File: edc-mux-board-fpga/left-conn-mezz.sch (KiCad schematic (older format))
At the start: 86 parts

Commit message: finished draft of horizontal pcb connector pinout.
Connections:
- net +12V: now also J?.37 (Pin_37), J?.38 (Pin_38); no longer J?.45 (Pin_45), J?.46 (Pin_46)
- net AUD_GND0: now also J?.5 (Pin_5); no longer J?.7 (Pin_7)
- net AUD_GND1: now also J?.17 (Pin_17); no longer J?.19 (Pin_19)
- net AUD_GND2: now also J?.29 (Pin_29); no longer J?.31 (Pin_31)
- net AUD_GND3: now also J?.51 (Pin_51); no longer J?.54 (Pin_54)
- net AUD_GND4: now also J?.63 (Pin_63); no longer J?.65 (Pin_65)
- net AUD_GND5: now also J?.75 (Pin_75); no longer J?.74 (Pin_74)
- net GND: now also J?.11 (Pin_11), J?.18 (Pin_18), J?.23 (Pin_23), J?.24 (Pin_24), J?.30 (Pin_30), J?.45 (Pin_45), J?.46 (Pin_46), J?.52 (Pin_52), J?.57 (Pin_57), J?.58 (Pin_58), J?.64 (Pin_64), J?.69 (Pin_69), J?.70 (Pin_70), J?.76 (Pin_76); no longer J?.1 (Pin_1), J?.13 (Pin_13), J?.22 (Pin_22), J?.25 (Pin_25), J?.33 (Pin_33), J?.37 (Pin_37), J?.38 (Pin_38), J?.47 (Pin_47), J?.48 (Pin_48), J?.49 (Pin_49), J?.59 (Pin_59), J?.68 (Pin_68), J?.75 (Pin_75), J?.80 (Pin_80)
- net ID_PIN0: now also J?.9 (Pin_9); no longer J?.10 (Pin_10)
- net ID_PIN1: now also J?.21 (Pin_21); no longer J?.20 (Pin_20)
- net ID_PIN2: now also J?.33 (Pin_33); no longer J?.26 (Pin_26)
- net ID_PIN3: now also J?.55 (Pin_55); no longer J?.51 (Pin_51)
- net ID_PIN4: now also J?.67 (Pin_67); no longer J?.60 (Pin_60)
- net ID_PIN5: now also J?.79 (Pin_79); no longer J?.71 (Pin_71)
- net INT_0: now also J?.7 (Pin_7); no longer J?.8 (Pin_8)
- net INT_1: now also J?.19 (Pin_19); no longer J?.18 (Pin_18)
- net INT_2: now also J?.31 (Pin_31); no longer J?.24 (Pin_24)
- net INT_4: now also J?.65 (Pin_65); no longer J?.62 (Pin_62)
- net INT_5: now also J?.77 (Pin_77); no longer J?.73 (Pin_73)
- net L_IN0: now also J?.3 (Pin_3); no longer J?.5 (Pin_5)
- net L_IN1: now also J?.15 (Pin_15); no longer J?.14 (Pin_14)
- net L_IN2: now also J?.27 (Pin_27); no longer J?.28 (Pin_28)
- net L_IN3: now also J?.49 (Pin_49); no longer J?.56 (Pin_56)
- net L_IN4: now also J?.61 (Pin_61); no longer J?.67 (Pin_67)
- net L_IN5: now also J?.73 (Pin_73); no longer J?.76 (Pin_76)
- net L_OUT0: now also J?.4 (Pin_4); no longer J?.2 (Pin_2)
- net L_OUT1: now also J?.16 (Pin_16); no longer J?.17 (Pin_17)
- net L_OUT2: now also J?.28 (Pin_28); no longer J?.32 (Pin_32)
- net L_OUT3: now also J?.50 (Pin_50); no longer J?.57 (Pin_57)
- net L_OUT4: now also J?.62 (Pin_62); no longer J?.64 (Pin_64)
- net L_OUT5: now also J?.74 (Pin_74); no longer J?.79 (Pin_79)
- net M_+12V: now also J?.37 (Pin_37), J?.38 (Pin_38); no longer J?.45 (Pin_45), J?.46 (Pin_46)
- net M_AUD_GND0: now also J?.5 (Pin_5); no longer J?.7 (Pin_7)
- net M_AUD_GND1: now also J?.17 (Pin_17); no longer J?.19 (Pin_19)
- net M_AUD_GND2: now also J?.29 (Pin_29); no longer J?.31 (Pin_31)
- net M_AUD_GND3: now also J?.51 (Pin_51); no longer J?.54 (Pin_54)
- net M_AUD_GND4: now also J?.63 (Pin_63); no longer J?.65 (Pin_65)
- net M_AUD_GND5: now also J?.75 (Pin_75); no longer J?.74 (Pin_74)
- net M_GND: now also J?.11 (Pin_11), J?.18 (Pin_18), J?.23 (Pin_23), J?.24 (Pin_24), J?.30 (Pin_30), J?.45 (Pin_45), J?.46 (Pin_46), J?.52 (Pin_52), J?.57 (Pin_57), J?.58 (Pin_58), J?.64 (Pin_64), J?.69 (Pin_69), J?.70 (Pin_70), J?.76 (Pin_76); no longer J?.1 (Pin_1), J?.13 (Pin_13), J?.22 (Pin_22), J?.25 (Pin_25), J?.33 (Pin_33), J?.37 (Pin_37), J?.38 (Pin_38), J?.47 (Pin_47), J?.48 (Pin_48), J?.49 (Pin_49), J?.59 (Pin_59), J?.68 (Pin_68), J?.75 (Pin_75), J?.80 (Pin_80)
- net M_ID_PIN0: now also J?.9 (Pin_9); no longer J?.10 (Pin_10)
- net M_ID_PIN1: now also J?.21 (Pin_21); no longer J?.20 (Pin_20)
- net M_ID_PIN2: now also J?.33 (Pin_33); no longer J?.26 (Pin_26)
- net M_ID_PIN3: now also J?.55 (Pin_55); no longer J?.51 (Pin_51)
- net M_ID_PIN4: now also J?.67 (Pin_67); no longer J?.60 (Pin_60)
- net M_ID_PIN5: now also J?.79 (Pin_79); no longer J?.71 (Pin_71)
- net M_INT_0: now also J?.7 (Pin_7); no longer J?.8 (Pin_8)
- net M_INT_1: now also J?.19 (Pin_19); no longer J?.18 (Pin_18)
- net M_INT_2: now also J?.31 (Pin_31); no longer J?.24 (Pin_24)
- net M_INT_4: now also J?.65 (Pin_65); no longer J?.62 (Pin_62)
- net M_INT_5: now also J?.77 (Pin_77); no longer J?.73 (Pin_73)
- net M_L_IN0: now also J?.3 (Pin_3); no longer J?.5 (Pin_5)
- net M_L_IN1: now also J?.15 (Pin_15); no longer J?.14 (Pin_14)
- net M_L_IN2: now also J?.27 (Pin_27); no longer J?.28 (Pin_28)
- net M_L_IN3: now also J?.49 (Pin_49); no longer J?.56 (Pin_56)
- net M_L_IN4: now also J?.61 (Pin_61); no longer J?.67 (Pin_67)
- net M_L_IN5: now also J?.73 (Pin_73); no longer J?.76 (Pin_76)
- net M_L_OUT1: now also J?.16 (Pin_16); no longer J?.15 (Pin_15)
- net M_L_OUT2: now also J?.28 (Pin_28); no longer J?.32 (Pin_32)
- net M_L_OUT3: now also J?.50 (Pin_50); no longer J?.57 (Pin_57)
- net M_L_OUT4: now also J?.62 (Pin_62); no longer J?.64 (Pin_64)
- net M_L_OUT5: now also J?.74 (Pin_74); no longer J?.79 (Pin_79)
- net M_R_IN0: now also J?.1 (Pin_1); no longer J?.3 (Pin_3)
- net M_R_IN1: now also J?.13 (Pin_13); no longer J?.16 (Pin_16)
- net M_R_IN2: now also J?.25 (Pin_25); no longer J?.30 (Pin_30)
- net M_R_IN3: now also J?.47 (Pin_47); no longer J?.58 (Pin_58)
- net M_R_IN4: now also J?.59 (Pin_59); no longer J?.69 (Pin_69)
- net M_R_IN5: now also J?.71 (Pin_71); no longer J?.78 (Pin_78)
- net M_R_OUT1: now also J?.14 (Pin_14); no longer J?.17 (Pin_17)
- net M_R_OUT2: now also J?.26 (Pin_26); no longer J?.34 (Pin_34)
- net M_R_OUT3: now also J?.48 (Pin_48); no longer J?.55 (Pin_55)
- net M_R_OUT4: now also J?.60 (Pin_60); no longer J?.66 (Pin_66)
- net M_R_OUT5: now also J?.72 (Pin_72); no longer J?.77 (Pin_77)
- net M_SCL_HV0: now also J?.8 (Pin_8); no longer J?.11 (Pin_11)
- net M_SCL_HV1: now also J?.20 (Pin_20); no longer J?.23 (Pin_23)
- net M_SCL_HV2: now also J?.32 (Pin_32); no longer J?.27 (Pin_27)
- net M_SCL_HV3: now also J?.54 (Pin_54); no longer J?.52 (Pin_52)
- net M_SCL_HV4: now also J?.66 (Pin_66); no longer J?.61 (Pin_61)
- net M_SCL_HV5: now also J?.78 (Pin_78); no longer J?.70 (Pin_70)
- net M_SDA_HV0: now also J?.10 (Pin_10); no longer J?.9 (Pin_9)
- net M_SDA_HV1: now also J?.22 (Pin_22); no longer J?.21 (Pin_21)
- net M_SDA_HV2: now also J?.34 (Pin_34); no longer J?.29 (Pin_29)
- net M_SDA_HV3: now also J?.56 (Pin_56); no longer J?.50 (Pin_50)
- net M_SDA_HV4: now also J?.68 (Pin_68); no longer J?.63 (Pin_63)
- net M_SDA_HV5: now also J?.80 (Pin_80); no longer J?.72 (Pin_72)
- net R_IN0: now also J?.1 (Pin_1); no longer J?.3 (Pin_3)
- net R_IN1: now also J?.13 (Pin_13); no longer J?.16 (Pin_16)
- net R_IN2: now also J?.25 (Pin_25); no longer J?.30 (Pin_30)
- net R_IN3: now also J?.47 (Pin_47); no longer J?.58 (Pin_58)
- net R_IN4: now also J?.59 (Pin_59); no longer J?.69 (Pin_69)
- net R_IN5: now also J?.71 (Pin_71); no longer J?.78 (Pin_78)
- net R_OUT0: now also J?.2 (Pin_2); no longer J?.4 (Pin_4)
- net R_OUT1: now also J?.14 (Pin_14); no longer J?.15 (Pin_15)
- net R_OUT2: now also J?.26 (Pin_26); no longer J?.34 (Pin_34)
- net R_OUT3: now also J?.48 (Pin_48); no longer J?.55 (Pin_55)
- net R_OUT4: now also J?.60 (Pin_60); no longer J?.66 (Pin_66)
- net R_OUT5: now also J?.72 (Pin_72); no longer J?.77 (Pin_77)
- net SCL_HV0: now also J?.8 (Pin_8); no longer J?.11 (Pin_11)
- net SCL_HV1: now also J?.20 (Pin_20); no longer J?.23 (Pin_23)
- net SCL_HV2: now also J?.32 (Pin_32); no longer J?.27 (Pin_27)
- net SCL_HV3: now also J?.54 (Pin_54); no longer J?.52 (Pin_52)
- net SCL_HV4: now also J?.66 (Pin_66); no longer J?.61 (Pin_61)
- net SCL_HV5: now also J?.78 (Pin_78); no longer J?.70 (Pin_70)
- net SDA_HV0: now also J?.10 (Pin_10); no longer J?.9 (Pin_9)
- net SDA_HV1: now also J?.22 (Pin_22); no longer J?.21 (Pin_21)
- net SDA_HV2: now also J?.34 (Pin_34); no longer J?.29 (Pin_29)
- net SDA_HV3: now also J?.56 (Pin_56); no longer J?.50 (Pin_50)
- net SDA_HV4: now also J?.68 (Pin_68); no longer J?.63 (Pin_63)
- net SDA_HV5: now also J?.80 (Pin_80); no longer J?.72 (Pin_72)
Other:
- moved on the sheet: C?, D?, F?, FB?, J?

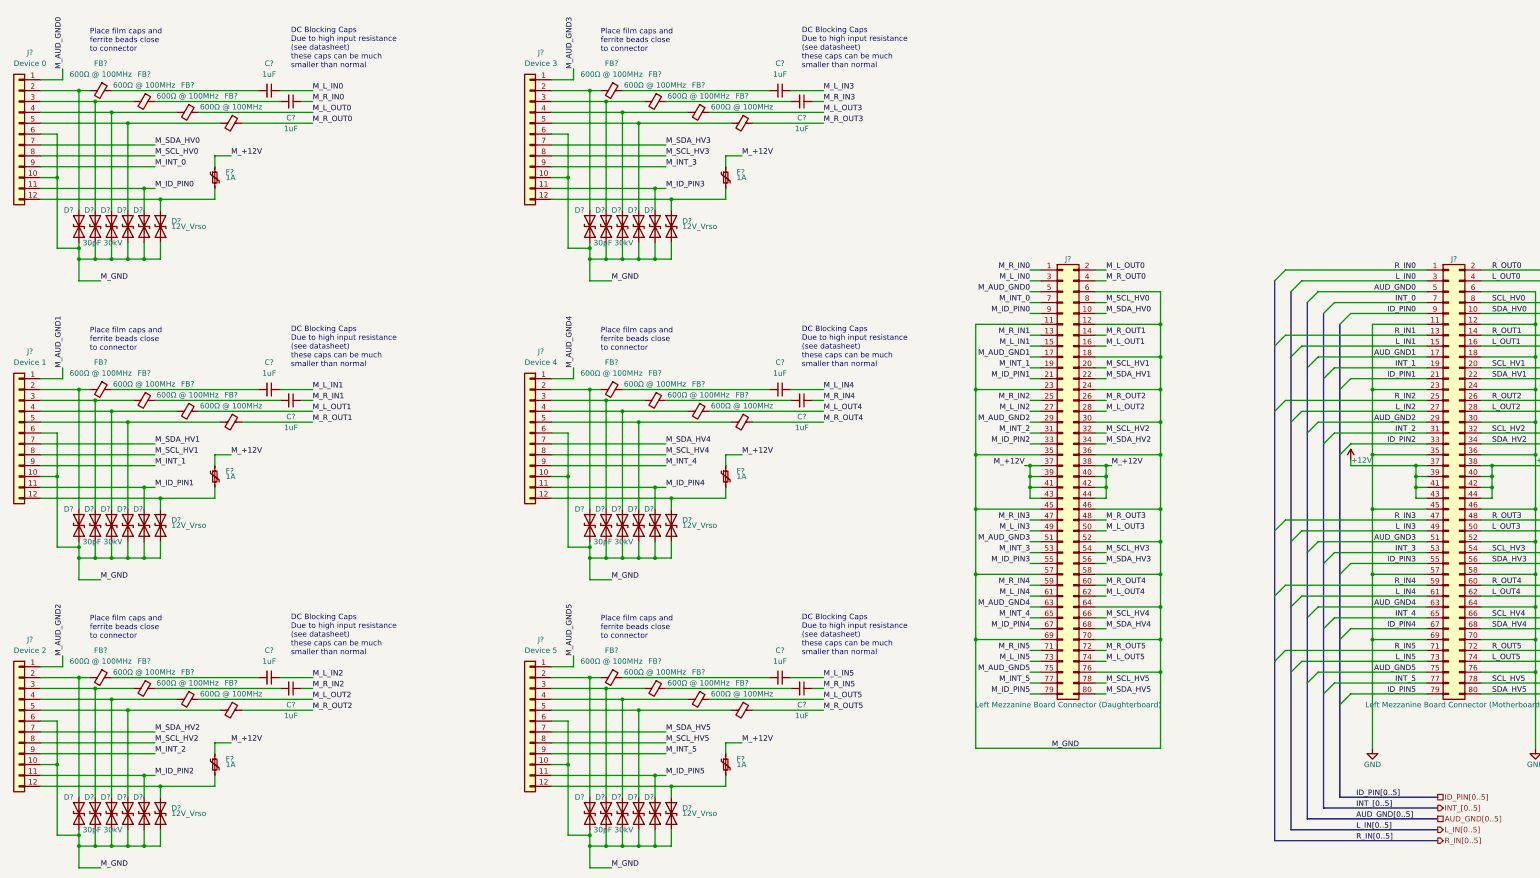
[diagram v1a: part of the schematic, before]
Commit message: Finished FPGA and MCU interconnections.
Finished up interrupt wiring
Fixed a few missing connections
Annotated Schematic
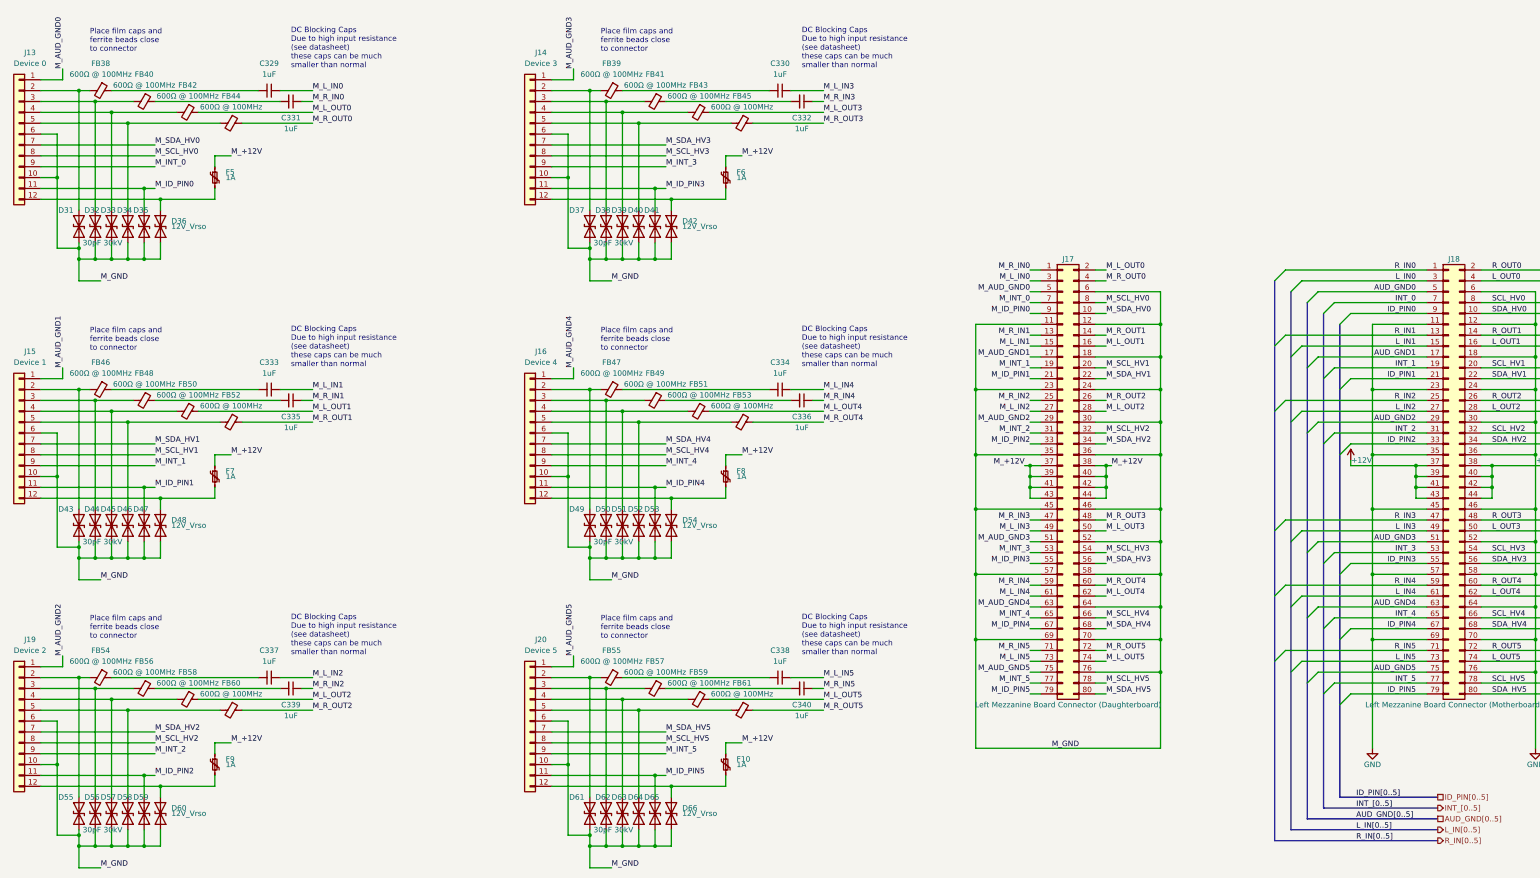
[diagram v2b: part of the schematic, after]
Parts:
- gave numbers to parts that had none: 86
